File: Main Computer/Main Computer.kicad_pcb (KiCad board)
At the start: 2 copper layers, 55.5 x 65.5 mm, 10 parts, among them J1 Pi 5 GPIO HEADER, J3 Conn_01x02, J4 CAN to outer connector, U2 E01-ML01DP5

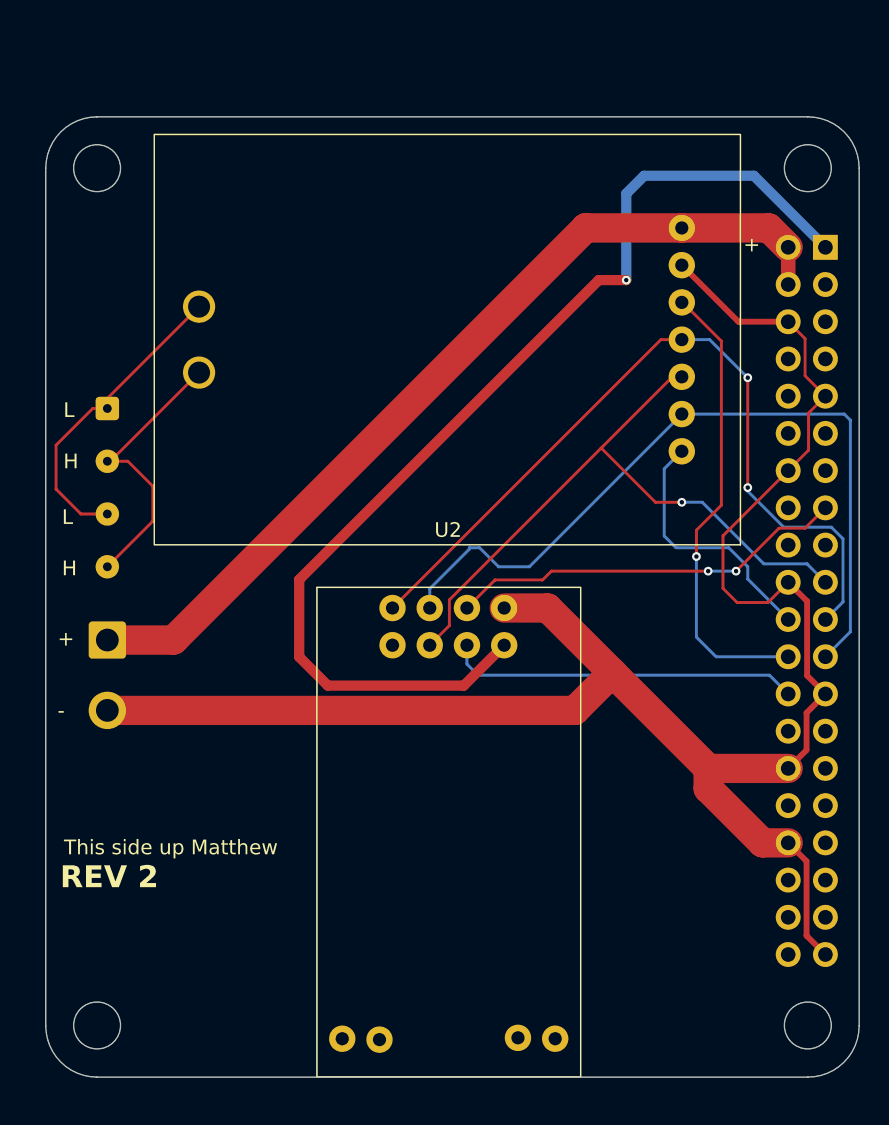
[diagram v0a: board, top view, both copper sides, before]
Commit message: need to align pinheader
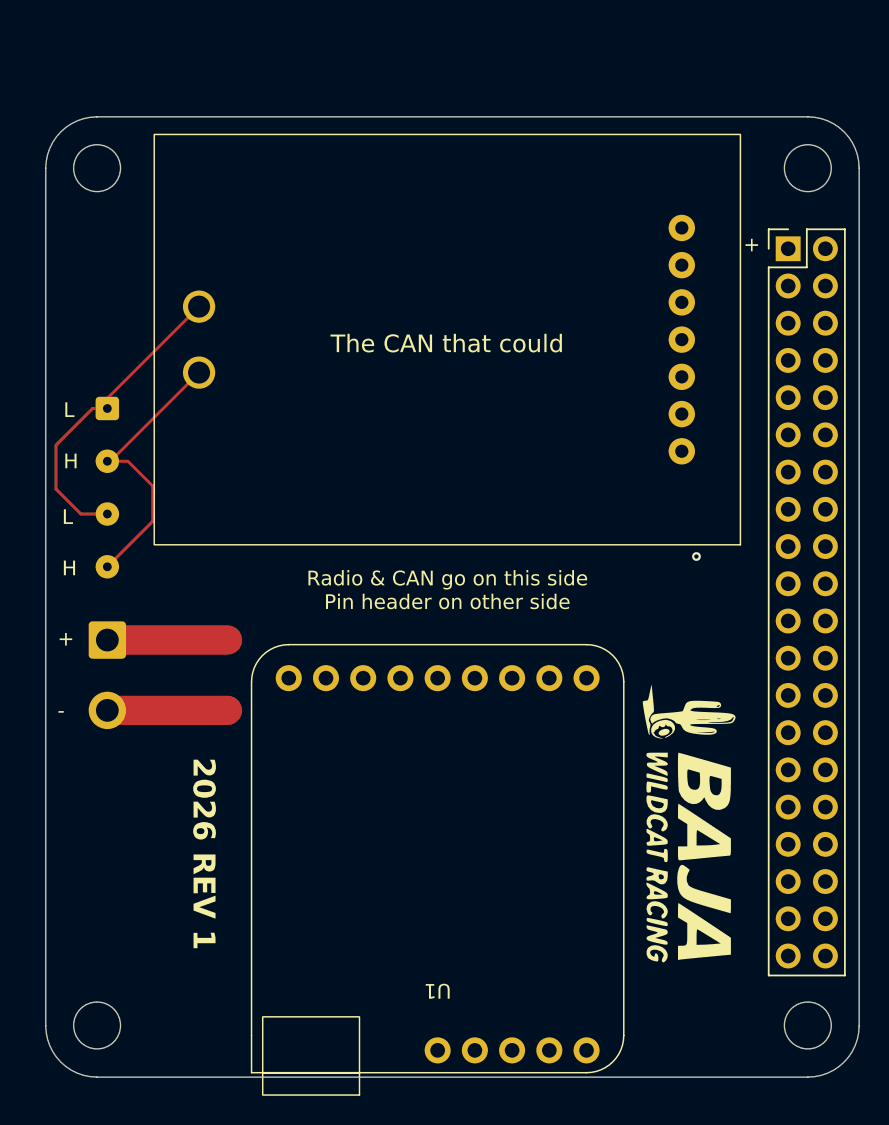
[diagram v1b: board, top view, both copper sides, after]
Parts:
- removed U2: E01-ML01DP5, 0_custom:Ebyte E01-ML01DP5
- added U1: RFM9X Breakout, Baja SAE Footprints:Adafruit RFM95W Breakout, F.Cu at (122.8, 158.1)
- G***, J1: moved to F.Cu
- moved G*** 37.4 mm to (140.0, 136.0), turned to -90 degrees
- moved J1 2.54 mm to (146.8, 96.8), turned to 0 degrees
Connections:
- J1 pad 15: CE -> unconnected-(J1-GPIO_22-Pad15)
- J1 pad 29: unconnected-(J1-GPIO_5-Pad29) -> RADIO_INT
- J1 pad 31: unconnected-(J1-GPIO_6-Pad31) -> RST
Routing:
- net GND: track 127.7 -> 8.20 mm
- net 3V3: track 74.0 -> 0.00 mm, vias 1 -> 0
- net SO: track 54.5 -> 0.00 mm, vias 2 -> 0
- net SCK: track 53.1 -> 0.02 mm
- net +5v: track 61.2 -> 8.20 mm
- net SI: track 44.9 -> 0.64 mm, vias 1 -> 0
- net CS: track 31.5 -> 0.06 mm
- net CE: track 27.3 -> 0.00 mm, vias 2 -> 0
- net CSN: track 24.0 -> 0.00 mm
- net INT: track 17.6 -> 0.00 mm
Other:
- board text added: "2026 REV 1"
- board text added: "Radio & CAN go on this side Pin header on other side"
- board text added: "The CAN that could"
- board text removed: "REV 2"
- board text removed: "This side up Matthew"

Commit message: routing done
still need to make can attachment holes bigger
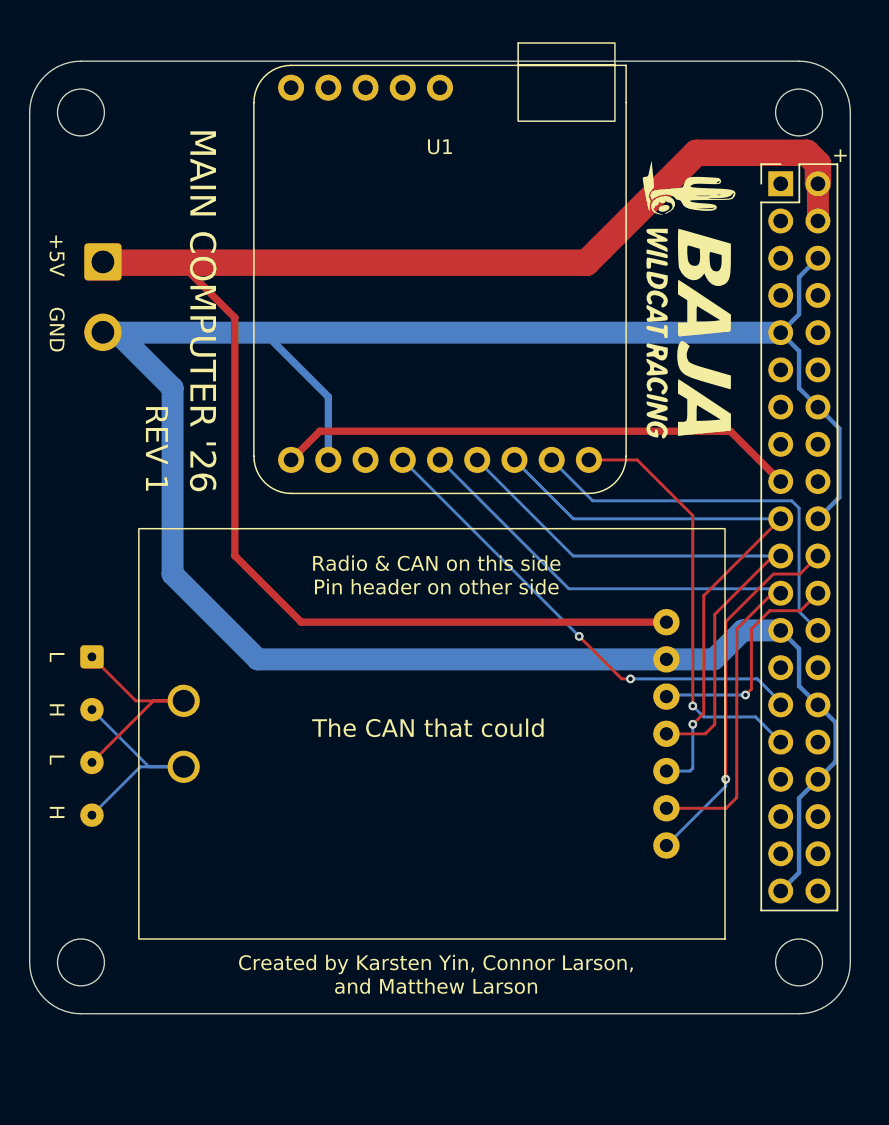
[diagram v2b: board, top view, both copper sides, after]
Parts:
- moved U1 78.9 mm to (123.0, 79.2), turned to 0 degrees
- moved REF** 62.3 mm to (98.5, 87.5)
- moved REF** 54.2 mm to (98.5, 145.5)
- moved G*** 35.8 mm to (140.0, 100.2)
- moved UNIT_1 26.9 mm to (128.5, 127.5)
- moved J3 25.8 mm to (100.0, 97.7)
- moved J4 17.0 mm to (99.2, 124.7)
- moved J1 4.46 mm to (146.2, 92.4)
- moved REF** 4.34 mm to (147.5, 145.5)
- moved REF** 3.85 mm to (147.5, 87.5)
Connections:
- J1 pad 1: 3V3 -> unconnected-(J1-3V3-Pad1)
- J1 pad 17: unconnected-(J1-3V3-Pad17) -> 3V3
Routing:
- net GND: track 8.20 -> 167.4 mm
- net +5v: track 8.20 -> 108.7 mm
- net SCK: track 0.02 -> 47.6 mm
- net SO: track 0.00 -> 40.6 mm
- net SI: track 0.64 -> 41.2 mm, vias 0 -> 1
- net 3V3: track 0.00 -> 35.6 mm
- net RADIO_INT: track 0.00 -> 32.8 mm, vias 0 -> 2
- net RST: track 0.00 -> 28.7 mm, vias 0 -> 1
- net CSN: track 0.00 -> 27.1 mm
- net INT: track 0.00 -> 25.1 mm, vias 0 -> 1
- net CS: track 0.06 -> 15.7 mm
- net Low: track 21.3 -> 15.5 mm
- net High: track 19.4 -> 15.5 mm
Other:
- board size 55.5 x 65.5 mm -> 56 x 65 mm
- board text added: "+5V"
- board text added: "Created by Karsten Yin, Connor Larson, and Matthew Larson"
- board text added: "GND"
- board text added: "MAIN COMPUTER '26"
- board text added: "REV 1"
- board text added: "Radio & CAN on this side Pin header on other side"
- board text removed: "-"
- board text removed: "2026 REV 1"
- board text removed: "Designed by Connor & Matthew Larson in Tucson, AZ"
- board text removed: "MAIN COMPUTER"
- board text removed: "Radio & CAN go on this side Pin header on other side"

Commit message: ready to submit
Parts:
- added G***: LOGO, 0_custom:wide_enough, B.Cu at (123.4, 104.3)
- J3: footprint Connector_Wire:SolderWire-0.75sqmm_1x02_P4.8mm_D1.25mm_OD2.3mm -> Connector_Wire:SolderWire-1.5sqmm_1x02_P7.8mm_D1.7mm_OD3.9mm
- J4: footprint Connector_Wire:SolderWire-0.1sqmm_1x04_P3.6mm_D0.4mm_OD1mm -> Connector_Wire:SolderWire-0.5sqmm_1x04_P4.6mm_D0.9mm_OD2.1mm
- moved U1 74.8 mm to (117.6, 153.8), turned to 180 degrees
- moved G*** 38.3 mm to (134.5, 138.2), turned to 90 degrees
- moved J4 27.5 mm to (99.5, 97.2)
- moved J3 26.4 mm to (100.2, 124.0)
- moved UNIT_1 26.1 mm to (127.8, 101.4)
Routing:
- net GND: track 167.4 -> 143.4 mm
- net +5v: track 108.7 -> 88.0 mm
- net RST: track 28.7 -> 44.9 mm, vias 1 -> 0
- net INT: track 25.1 -> 11.1 mm, vias 1 -> 0
- net 3V3: track 35.6 -> 22.3 mm
- net CSN: track 27.1 -> 40.3 mm, vias 0 -> 1
- net CS: track 15.7 -> 28.3 mm, vias 1 -> 0
- net SO: track 40.6 -> 52.6 mm
- net SCK: track 47.6 -> 41.7 mm, vias 0 -> 1
- net SI: track 41.2 -> 45.6 mm
- net RADIO_INT: track 32.8 -> 29.8 mm, vias 2 -> 0
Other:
- board text added: "MAIN COMPUTER '26 REV 1"
- board text removed: "MAIN COMPUTER '26"
- board text removed: "REV 1"

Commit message: update stuff, fix error
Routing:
- net RADIO_INT: track 29.8 -> 28.8 mm

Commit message: workprogress
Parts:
- J3: footprint Connector_Wire:SolderWire-1.5sqmm_1x02_P7.8mm_D1.7mm_OD3.9mm -> Connector_Wire:SolderWire-0.75sqmm_1x02_P4.8mm_D1.25mm_OD2.3mm
- J4: footprint Connector_Wire:SolderWire-0.5sqmm_1x04_P4.6mm_D0.9mm_OD2.1mm -> Connector_Wire:SolderWire-0.1sqmm_1x04_P3.6mm_D0.4mm_OD1mm
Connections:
- J1 pad 15: unconnected-(J1-GPIO_22-Pad15) -> CAN_INT
- J1 pad 22: INT -> unconnected-(J1-GPIO_25-Pad22)
- J1 pad 24: CS -> unconnected-(J1-GPIO_8-Pad24)
- J1 pad 35: unconnected-(J1-GPIO_19-Pad35) -> SPI1_MISO
- J1 pad 36: unconnected-(J1-GPIO_16-Pad36) -> CAN_CS
- J1 pad 38: unconnected-(J1-GPIO_20-Pad38) -> SPI1_MOSI
- J1 pad 40: unconnected-(J1-GPIO_21-Pad40) -> SPI1_SCK
- UNIT_1 pad 1: INT -> CAN_INT
- UNIT_1 pad 2: SCK -> SPI1_SCK
- UNIT_1 pad 3: SI -> SPI1_MOSI
- UNIT_1 pad 4: SO -> SPI1_MISO
- UNIT_1 pad 5: CS -> CAN_CS
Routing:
- net CS: track 28.3 -> 0.00 mm
- net SO: track 52.6 -> 33.8 mm, vias 0 -> 1
- net INT: track 11.1 -> 0.00 mm
- net SCK: track 41.7 -> 31.7 mm
- net SI: track 45.6 -> 36.5 mm
- net GND: track 143.4 -> 134.7 mm
- net 3V3: track 22.3 -> 25.7 mm
- net RST: track 44.9 -> 44.0 mm
- net CAN_CS: track 0.00 -> 0.71 mm
- net SPI1_MISO: track 0.00 -> 0.55 mm

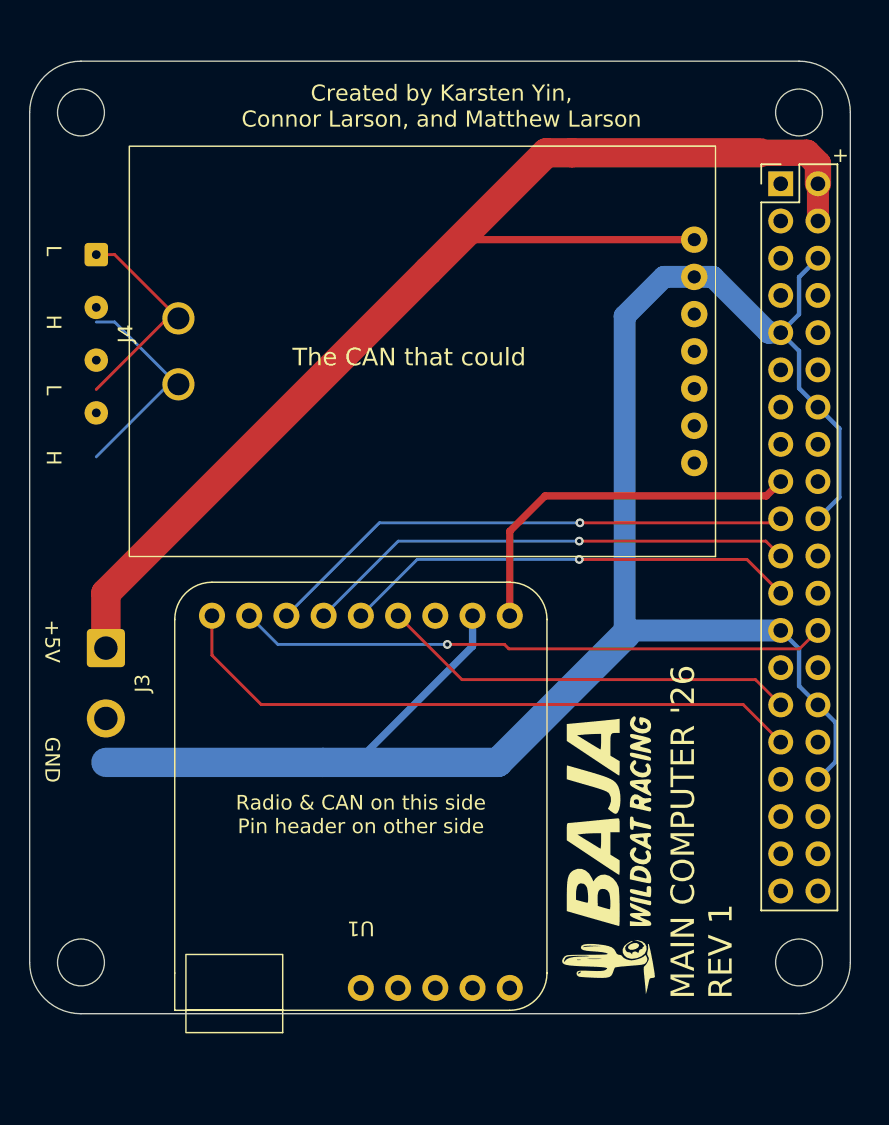
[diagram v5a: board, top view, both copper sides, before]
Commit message: Revert only PCB this time
This reverts some of commit 10dbf7cf734bf138f5810b545ad3c613d1decc14.
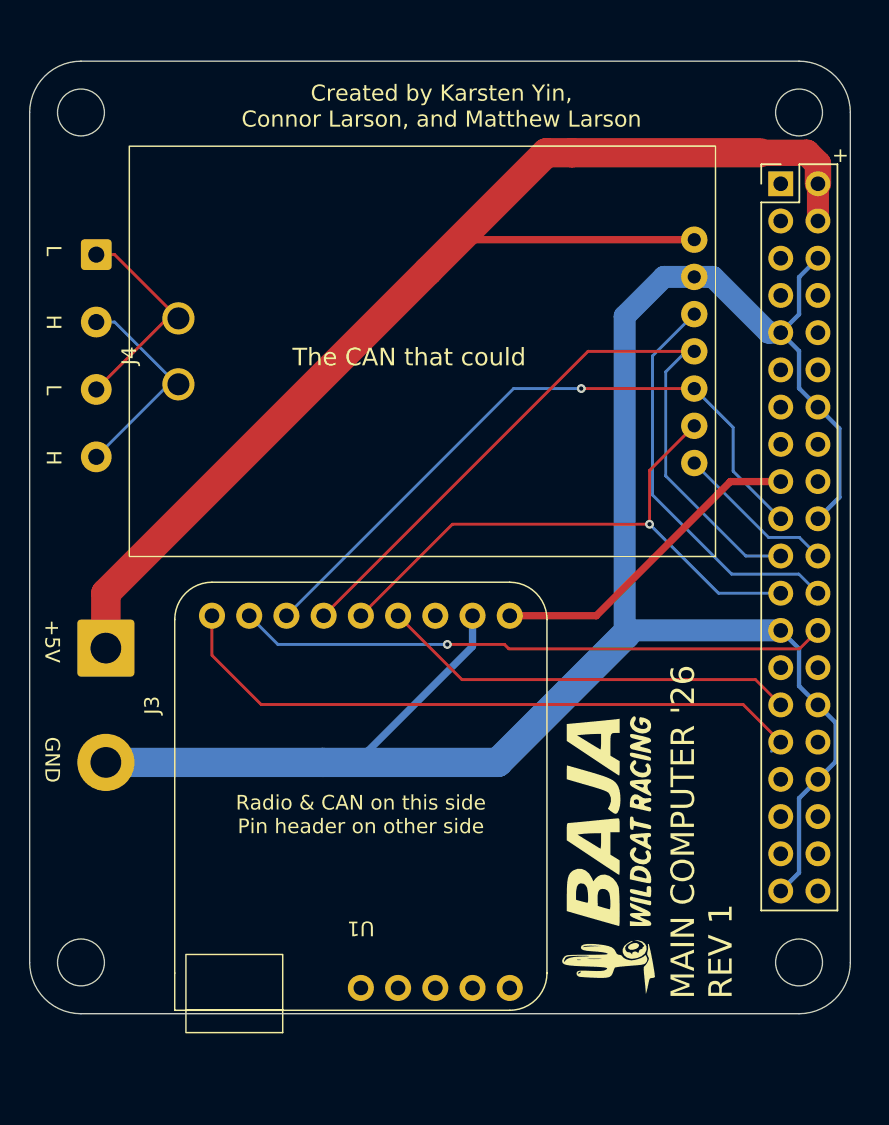
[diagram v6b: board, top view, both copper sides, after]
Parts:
- J3: footprint Connector_Wire:SolderWire-0.75sqmm_1x02_P4.8mm_D1.25mm_OD2.3mm -> Connector_Wire:SolderWire-1.5sqmm_1x02_P7.8mm_D1.7mm_OD3.9mm
- J4: footprint Connector_Wire:SolderWire-0.1sqmm_1x04_P3.6mm_D0.4mm_OD1mm -> Connector_Wire:SolderWire-0.5sqmm_1x04_P4.6mm_D0.9mm_OD2.1mm
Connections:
- J1 pad 15: CAN_INT -> unconnected-(J1-GPIO_22-Pad15)
- J1 pad 22: unconnected-(J1-GPIO_25-Pad22) -> INT
- J1 pad 24: unconnected-(J1-GPIO_8-Pad24) -> CS
- J1 pad 35: SPI1_MISO -> unconnected-(J1-GPIO_19-Pad35)
- J1 pad 36: CAN_CS -> unconnected-(J1-GPIO_16-Pad36)
- J1 pad 38: SPI1_MOSI -> unconnected-(J1-GPIO_20-Pad38)
- J1 pad 40: SPI1_SCK -> unconnected-(J1-GPIO_21-Pad40)
- UNIT_1 pad 1: CAN_INT -> INT
- UNIT_1 pad 2: SPI1_SCK -> SCK
- UNIT_1 pad 3: SPI1_MOSI -> SI
- UNIT_1 pad 4: SPI1_MISO -> SO
- UNIT_1 pad 5: CAN_CS -> CS
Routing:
- net CS: track 0.00 -> 28.3 mm
- net SO: track 33.8 -> 52.6 mm, vias 1 -> 0
- net INT: track 0.00 -> 11.1 mm
- net SCK: track 31.7 -> 41.7 mm
- net SI: track 36.5 -> 45.6 mm
- net GND: track 134.7 -> 143.4 mm
- net 3V3: track 25.7 -> 22.3 mm
- net RST: track 44.0 -> 44.9 mm
- net CAN_CS: track 0.71 -> 0.00 mm
- net SPI1_MISO: track 0.55 -> 0.00 mm

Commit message: PCB KNOWN GOOD
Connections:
- J1 pad 15: unconnected-(J1-GPIO_22-Pad15) -> CAN_INT
- J1 pad 22: INT -> unconnected-(J1-GPIO_25-Pad22)
- J1 pad 24: CS -> unconnected-(J1-GPIO_8-Pad24)
- J1 pad 35: unconnected-(J1-GPIO_19-Pad35) -> SPI1_MISO
- J1 pad 36: unconnected-(J1-GPIO_16-Pad36) -> CAN_CS
- J1 pad 38: unconnected-(J1-GPIO_20-Pad38) -> SPI1_MOSI
- J1 pad 40: unconnected-(J1-GPIO_21-Pad40) -> SPI1_SCK
- UNIT_1 pad 1: INT -> CAN_INT
- UNIT_1 pad 2: SCK -> SPI1_SCK
- UNIT_1 pad 3: SI -> SPI1_MOSI
- UNIT_1 pad 4: SO -> SPI1_MISO
- UNIT_1 pad 5: CS -> CAN_CS
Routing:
- net SO: track 52.6 -> 0.05 mm
- net SI: track 45.6 -> 0.00 mm, vias 1 -> 0
- net SCK: track 41.7 -> 0.54 mm, vias 1 -> 0
- net CS: track 28.3 -> 0.00 mm
- net INT: track 11.1 -> 0.00 mm
- net GND: track 143.4 -> 134.7 mm
- net RST: track 44.9 -> 44.0 mm
- net CAN_CS: track 0.00 -> 0.71 mm
- net SPI1_MISO: track 0.00 -> 0.55 mm

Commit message: rev 2 almost done
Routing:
- net SPI1_SCK: track 0.00 -> 40.1 mm, vias 0 -> 2
- net CAN_CS: track 0.71 -> 40.0 mm, vias 0 -> 2
- net SPI1_MOSI: track 0.00 -> 37.0 mm, vias 0 -> 2
- net SI: track 0.00 -> 36.5 mm, vias 0 -> 1
- net SPI1_MISO: track 0.55 -> 35.6 mm, vias 0 -> 2
- net SO: track 0.05 -> 33.8 mm, vias 0 -> 1
- net SCK: track 0.54 -> 31.5 mm, vias 0 -> 1
- net GND: track 134.7 -> 143.4 mm
- net CAN_INT: track 0.00 -> 6.43 mm
- net CSN: track 40.3 -> 43.7 mm
- net 3V3: track 22.3 -> 25.4 mm
